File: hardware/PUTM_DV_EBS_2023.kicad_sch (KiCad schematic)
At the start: 0 parts

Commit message: Dimensions compress, routing
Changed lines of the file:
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@@
     (stroke (width 0) (type default))
   )
-  (wire (pts (xy 140.97 96.52) (xy 140.97 106.68))
+  (wire (pts (xy 142.24 96.52) (xy 142.24 106.68))
+    (stroke (width 0) (type default))
+  )
+  (wire (pts (xy 177.8 74.93) (xy 207.01 74.93))
     (stroke (width 0) (type default))
   )
@@
     (stroke (width 0) (type default))
   )
-  (wire (pts (xy 255.27 41.91) (xy 255.27 59.69))
+  (wire (pts (xy 177.8 78.74) (xy 207.01 78.74))
     (stroke (width 0) (type default))
   )
-  (wire (pts (xy 177.8 78.74) (xy 213.36 78.74))
+  (wire (pts (xy 255.27 41.91) (xy 255.27 59.69))
     (stroke (width 0) (type default))
   )
-  (wire (pts (xy 52.07 138.43) (xy 110.49 138.43))
+  (wire (pts (xy 52.07 138.43) (xy 111.76 138.43))
     (stroke (width 0) (type default))
   )
@@
     (stroke (width 0) (type default))
   )
-  (wire (pts (xy 52.07 138.43) (xy 38.1 138.43))
+  (wire (pts (xy 177.8 83.82) (xy 207.01 83.82))
     (stroke (width 0) (type default))
   )
-  (wire (pts (xy 177.8 74.93) (xy 213.36 74.93))
+  (wire (pts (xy 52.07 138.43) (xy 38.1 138.43))
     (stroke (width 0) (type default))
   )
@@
     (stroke (width 0) (type default))
   )
-  (wire (pts (xy 148.59 127) (xy 199.39 127))
+  (wire (pts (xy 149.86 127) (xy 207.01 127))
+    (stroke (width 0) (type default))
+  )
+  (wire (pts (xy 177.8 64.77) (xy 207.01 64.77))
     (stroke (width 0) (type default))
   )
@@
     (stroke (width 0) (type default))
   )
-  (wire (pts (xy 177.8 83.82) (xy 213.36 83.82))
-    (stroke (width 0) (type default))
-  )
-  (wire (pts (xy 257.81 107.95) (xy 257.81 121.92))
+  (wire (pts (xy 267.97 107.95) (xy 267.97 121.92))
     (stroke (width 0) (type default))
   )
@@
     (stroke (width 0) (type default))
   )
-  (wire (pts (xy 251.46 107.95) (xy 251.46 121.92))
-    (stroke (width 0) (type default))
-  )
-  (wire (pts (xy 177.8 64.77) (xy 213.36 64.77))
+  (wire (pts (xy 262.89 107.95) (xy 262.89 121.92))
     (stroke (width 0) (type default))
   )
@@
     (stroke (width 0) (type default))
   )
-  (wire (pts (xy 148.59 138.43) (xy 161.29 138.43))
+  (wire (pts (xy 149.86 138.43) (xy 161.29 138.43))
     (stroke (width 0) (type default))
   )
@@
     )
   )
-  (image (at 147.32 31.75) (scale 0.190884)
+  (image (at 133.35 31.75) (scale 0.190884)
     (data
       iVBORw0KGgoAAAANSUhEUgAABAIAAAUACAIAAABS/WddAAAAA3NCSVQICAjb4U/gAAAgAElEQVR4
@@
     )
   )
-  (image (at 232.41 140.97)
+  (image (at 242.57 140.97)
     (data
       iVBORw0KGgoAAAANSUhEUgAAAYgAAAGoCAIAAADTjeVHAAAAA3NCSVQICAjb4U/gAAAACXBIWXMA
@@
       (effects (font (size 1.27 1.27)) (justify right))
     )
-    (pin "SAFETY_RELAY_CTRL" output (at 140.97 96.52 270)
+    (pin "SAFETY_RELAY_CTRL" output (at 142.24 96.52 270)
       (effects (font (size 1.27 1.27)) (justify left))
     )
@@
     )
   )
-  (sheet (at 199.39 121.92) (size 60.96 38.1)
+  (sheet (at 207.01 121.92) (size 72.39 38.1)
     (stroke (width 0.1524) (type solid))
     (fill (color 0 0 0 0.0000))
-    (property "Sheetname" "Solenoid Control and Supply" (at 200.66 121.92 0)
+    (property "Sheetname" "Solenoid Control and Supply" (at 208.28 121.92 0)
       (effects (font (size 1.27 1.27)) (justify left bottom))
     )
-    (property "Sheetfile" "output.kicad_sch" (at 201.93 161.29 0)
+    (property "Sheetfile" "output.kicad_sch" (at 209.55 161.29 0)
       (effects (font (size 1.27 1.27)) (justify left top))
     )
-    (pin "VALVE_2_SIG" input (at 251.46 121.92 90)
+    (pin "VALVE_2_SIG" input (at 262.89 121.92 90)
       (effects (font (size 1.27 1.27)) (justify right))
     )
-    (pin "VALVE_1_SIG" input (at 257.81 121.92 90)
+    (pin "VALVE_1_SIG" input (at 267.97 121.92 90)
       (effects (font (size 1.27 1.27)) (justify right))
     )
-    (pin "VALVE_SUPPLY" input (at 199.39 127 180)
+    (pin "VALVE_SUPPLY" input (at 207.01 127 180)
       (effects (font (size 1.27 1.27)) (justify left))
     )
@@
     )
   )
-  (sheet (at 110.49 106.68) (size 38.1 40.64) (fields_autoplaced)
+  (sheet (at 111.76 106.68) (size 38.1 40.64) (fields_autoplaced)
     (stroke (width 0.1524) (type solid))
     (fill (color 0 0 0 0.0000))
-    (property "Sheetname" "Safety Relay" (at 110.49 105.9684 0)
+    (property "Sheetname" "Safety Relay" (at 111.76 105.9684 0)
       (effects (font (size 1.27 1.27)) (justify left bottom))
     )
-    (property "Sheetfile" "latch.kicad_sch" (at 110.49 147.9046 0)
+    (property "Sheetfile" "latch.kicad_sch" (at 111.76 147.9046 0)
       (effects (font (size 1.27 1.27)) (justify left top))
     )
-    (pin "SAFE_OUT" output (at 148.59 138.43 0)
+    (pin "SAFE_OUT" output (at 149.86 138.43 0)
       (effects (font (size 1.27 1.27)) (justify right))
     )
-    (pin "SAFETY_RELAY" input (at 140.97 106.68 90)
+    (pin "SAFETY_RELAY" input (at 142.24 106.68 90)
       (effects (font (size 1.27 1.27)) (justify right))
     )
-    (pin "SAFE_IN" input (at 110.49 138.43 180)
+    (pin "SAFE_IN" input (at 111.76 138.43 180)
       (effects (font (size 1.27 1.27)) (justify left))
     )
-    (pin "VALVE_SUPPLY" output (at 148.59 127 0)
+    (pin "VALVE_SUPPLY" output (at 149.86 127 0)
       (effects (font (size 1.27 1.27)) (justify right))
     )
@@
     )
   )
-  (sheet (at 213.36 59.69) (size 59.69 48.26)
+  (sheet (at 207.01 59.69) (size 72.39 48.26)
     (stroke (width 0.1524) (type solid))
     (fill (color 0 0 0 0.0000))
-    (property "Sheetname" "EBS Supervisor" (at 213.36 58.9784 0)
+    (property "Sheetname" "EBS Supervisor" (at 207.01 58.9784 0)
       (effects (font (size 1.27 1.27)) (justify left bottom))
     )
-    (property "Sheetfile" "supervisor.kicad_sch" (at 205.74 107.95 0)
+    (property "Sheetfile" "supervisor.kicad_sch" (at 199.39 107.95 0)
       (effects (font (size 1.27 1.27)) (justify left top))
     )
-    (pin "WATCHDOG" output (at 213.36 78.74 180)
+    (pin "WATCHDOG" output (at 207.01 78.74 180)
       (effects (font (size 1.27 1.27)) (justify left))
     )
-    (pin "SDC_READY" input (at 213.36 64.77 180)
+    (pin "SDC_READY" input (at 207.01 64.77 180)
       (effects (font (size 1.27 1.27)) (justify left))
     )
-    (pin "AS_CLOSE_SDC" output (at 213.36 74.93 180)
+    (pin "AS_CLOSE_SDC" output (at 207.01 74.93 180)
       (effects (font (size 1.27 1.27)) (justify left))
     )
-    (pin "VALVE_1" output (at 257.81 107.95 270)
+    (pin "VALVE_1" output (at 267.97 107.95 270)
       (effects (font (size 1.27 1.27)) (justify left))
     )
-    (pin "VALVE_2" output (at 251.46 107.95 270)
+    (pin "VALVE_2" output (at 262.89 107.95 270)
       (effects (font (size 1.27 1.27)) (justify left))
     )
@@
       (effects (font (size 1.27 1.27)) (justify right))
     )
-    (pin "WD_ready" input (at 213.36 83.82 180)
+    (pin "WD_ready" input (at 207.01 83.82 180)
       (effects (font (size 1.27 1.27)) (justify left))
     )
@@
     )
   )
-  (sheet (at 125.73 17.78) (size 44.45 30.48) (fields_autoplaced)
+  (sheet (at 111.76 17.78) (size 44.45 30.48) (fields_autoplaced)
     (stroke (width 0.1524) (type solid))
     (fill (color 0 0 0 0.0000))
-    (property "Sheetname" "Connector" (at 125.73 17.0684 0)
+    (property "Sheetname" "Connector" (at 111.76 17.0684 0)
       (effects (font (size 1.27 1.27)) (justify left bottom))
     )
-    (property "Sheetfile" "connector.kicad_sch" (at 125.73 48.8446 0)
+    (property "Sheetfile" "connector.kicad_sch" (at 111.76 48.8446 0)
       (effects (font (size 1.27 1.27)) (justify left top))
     )

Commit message: replace RES2 input to actuator relai
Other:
- sheet Safety Relay ports: added none; removed VALVE_SUPPLY
- sheet Solenoid Control and Supply ports: added none; removed VALVE_SUPPLY
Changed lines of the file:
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@@
     (stroke (width 0) (type default))
   )
-  (wire (pts (xy 149.86 127) (xy 207.01 127))
-    (stroke (width 0) (type default))
-  )
   (wire (pts (xy 177.8 64.77) (xy 207.01 64.77))
     (stroke (width 0) (type default))
@@
       (effects (font (size 1.27 1.27)) (justify right))
     )
-    (pin "VALVE_SUPPLY" input (at 207.01 127 180)
-      (effects (font (size 1.27 1.27)) (justify left))
-    )
     (instances
       (project "PUTM_DV_EBS_2023"
@@
       (effects (font (size 1.27 1.27)) (justify left))
     )
-    (pin "VALVE_SUPPLY" output (at 149.86 127 0)
-      (effects (font (size 1.27 1.27)) (justify right))
-    )
     (instances

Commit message: changed pcb version
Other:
- sheet Watchdog supervisor & SDC detection renamed EBS Logic
- sheet Air pressure sensor control ports: added none; removed PRESS4, SENSOR_SPARE
- sheet EBS Logic ports: added AS_DRIVING_MODE, SAFETY_OUT, SAFETY_RESET_BUT, SDC READY, TS_ON_COCKPIT, TS_ON_EXT; removed SAFETY_RELAY_CTRL, SDC_Status, WD_ready
- sheet EBS Supervisor ports: added AS_DRIVING_MODE; removed AIR_SPARE, WD_ready
- sheet Input Protection ports: added SAFETY_RESET_BUTT_P, TS_COCKPIT_P, TS_ON_EXT_P; removed none
- sheet Safety Relay ports: added VALVE_SUPPLY; removed none
- sheet Solenoid Control and Supply ports: added VALVE_SUPPLY; removed none

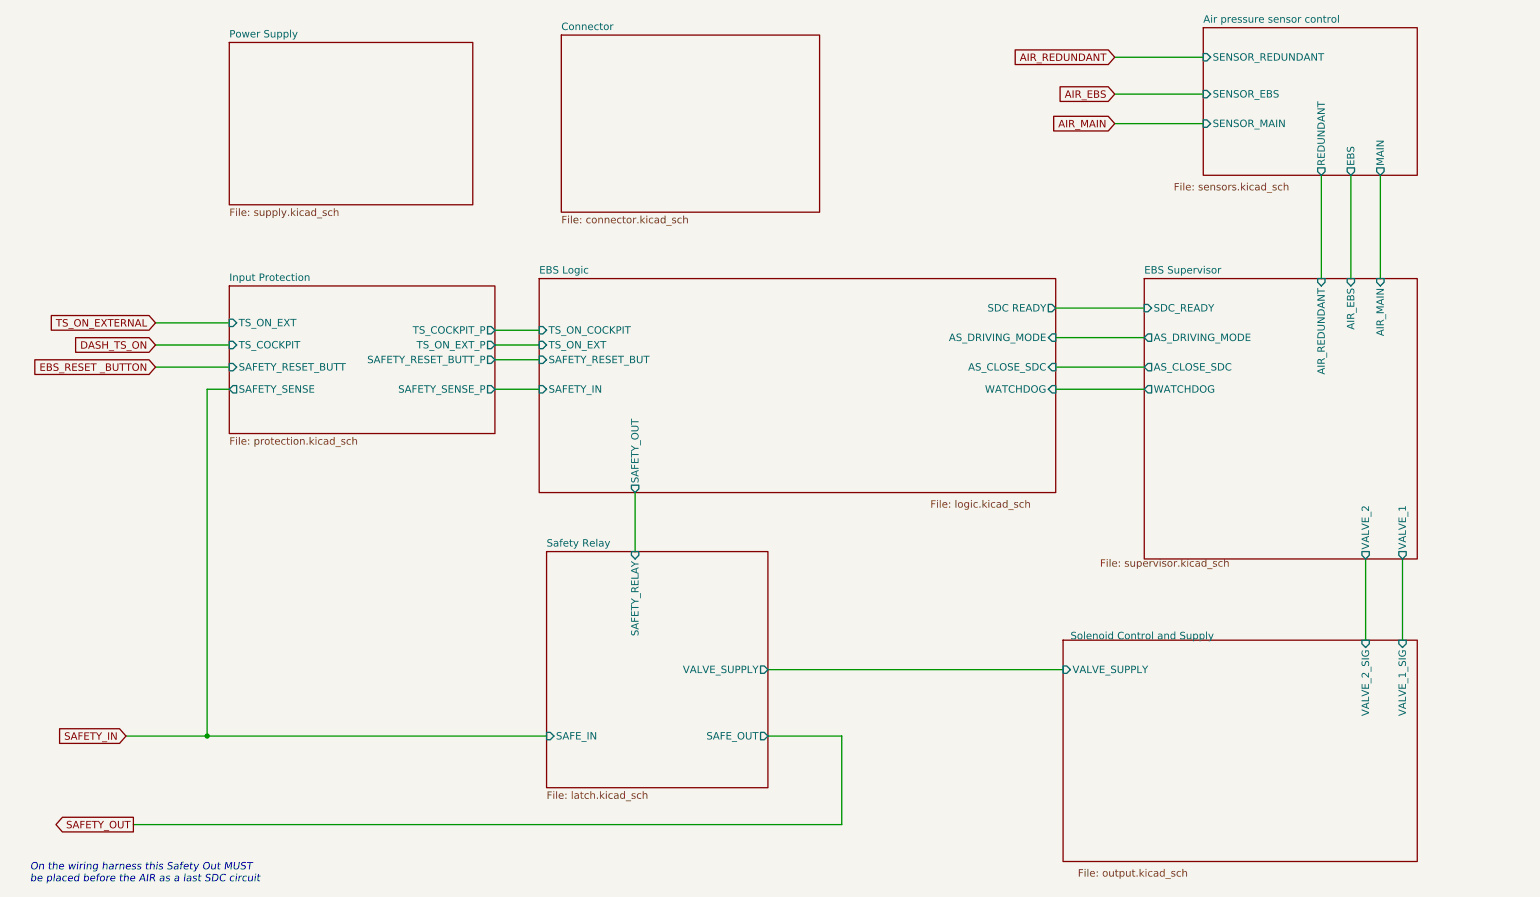
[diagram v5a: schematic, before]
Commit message: Schematic redesign for 23 rules, new pressure buffer, protection fix
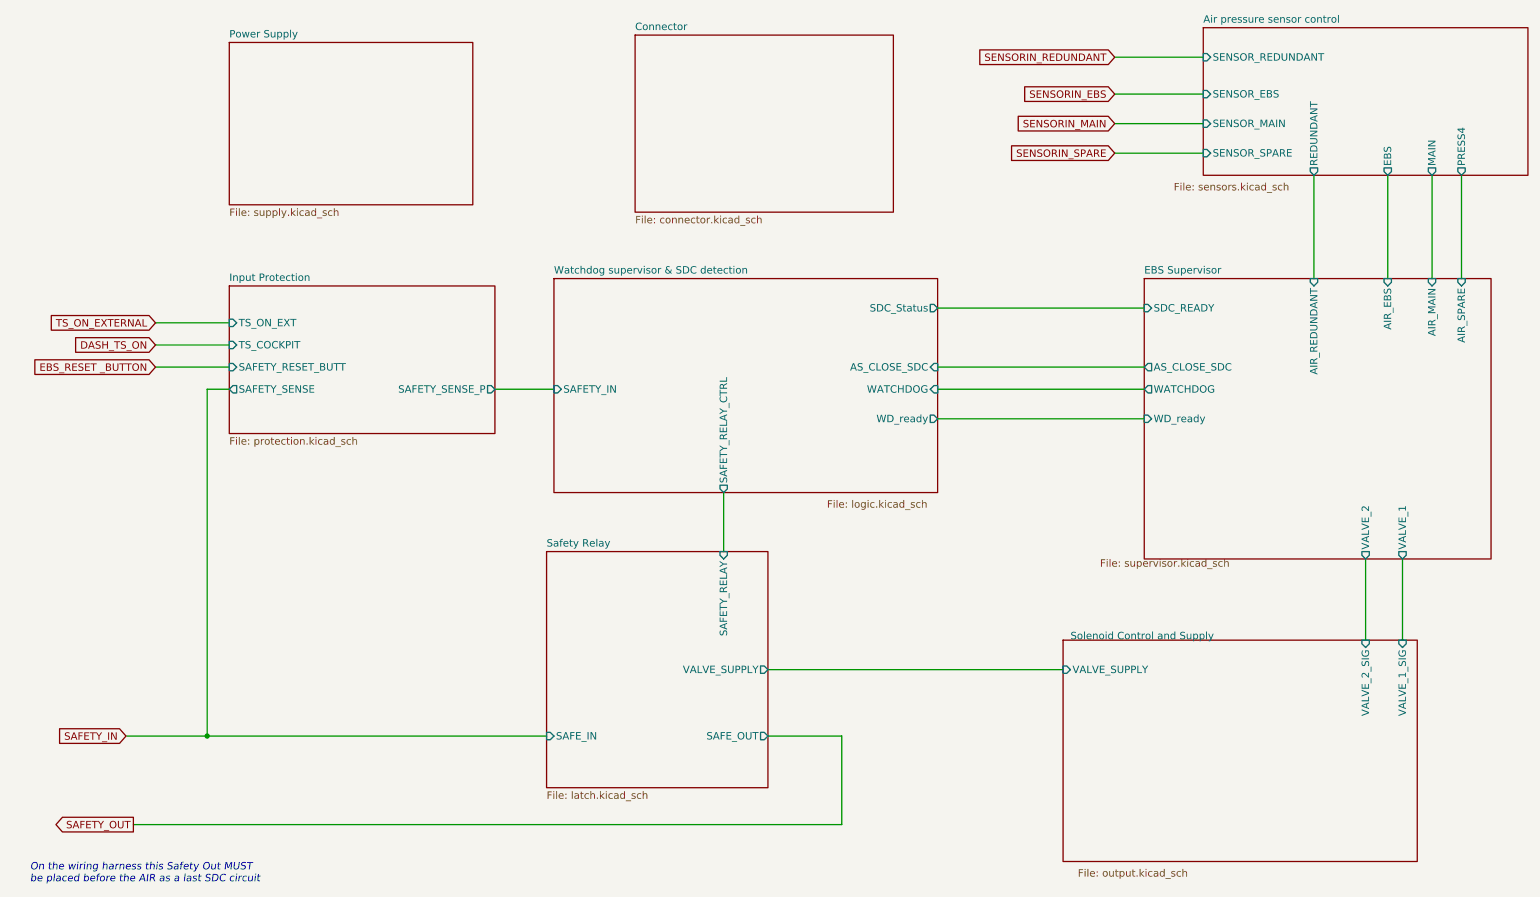
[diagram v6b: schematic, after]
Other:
- sheet EBS Logic renamed Watchdog supervisor & SDC detection
- sheet Air pressure sensor control ports: added PRESS4, SENSOR_SPARE; removed none
- sheet EBS Supervisor ports: added AIR_SPARE, WD_ready; removed AS_DRIVING_MODE
- sheet Input Protection ports: added none; removed SAFETY_RESET_BUTT_P, TS_COCKPIT_P, TS_ON_EXT_P
- sheet Watchdog supervisor & SDC detection ports: added SAFETY_RELAY_CTRL, SDC_Status, WD_ready; removed AS_DRIVING_MODE, SAFETY_OUT, SAFETY_RESET_BUT, SDC READY, TS_ON_COCKPIT, TS_ON_EXT
